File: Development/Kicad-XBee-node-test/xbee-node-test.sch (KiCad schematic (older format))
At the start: 41 parts, among them IC1 ATMEGA48-P

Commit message: Complete Kicad-XBee-node-test PCB to the layout stage. Added some jumpers to allow the board to be used in low power mode. Includes name change.
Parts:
- removed Q?: 2N7002, symbol MOSFET_N
- removed RV?: 10K, symbol POT
- removed U?: 78L05, symbol 78L05
- added Q1: 2N7002, photodiode:SOT23GDS, symbol MOSFET_N
- added R14: 1M, photodiode:SM0603_Resistor, symbol R
- added SW1: Reset, photodiode:SW_PUSH_TINY, symbol SW_Push
- added SW2: Commissioning, photodiode:SW_PUSH_TINY, symbol SW_Push
- added U1: TPS77033, photodiode:SOT23-5, symbol TPS77033
- added W1, W2, W3: Jumper, photodiode:SIL-2, symbol TEST_2P
- C1, C2, C3, C4, C5: renamed from C?; footprint (none) -> photodiode:SM0603_Capa
- C6, C7: renamed from C?; footprint (none) -> photodiode:SM1206POL
- D1: renamed from D?; footprint (none) -> photodiode:TO-92_LM336
- D2, D4, D6, D7: renamed from D?; footprint (none) -> photodiode:LED-5MM
- D3, D5: renamed from D?; footprint (none) -> photodiode:D_0603
- D8: renamed from D?; footprint (none) -> photodiode:D_SOD-323_HandSoldering
- IC1: footprint DIL28 -> photodiode:DIP-28
- L1, L2: renamed from L?; footprint (none) -> photodiode:R_0805
- P1: renamed from P?; footprint (none) -> photodiode:PINHEAD1-6
- P2, P3, P4: renamed from P?; footprint (none) -> photodiode:PINHEAD1-2
- Q2: renamed from Q?; footprint (none) -> photodiode:SOT23GDS
- R1, R10, R11, R12, R13, R2, R7, R8, R9: renamed from R?; footprint (none) -> photodiode:SM0603_Resistor
- R3, R4, R5, R6: renamed from R?; value 270 -> 470; footprint (none) -> photodiode:SM0603_Resistor
- RV1: renamed from RV?; footprint (none) -> photodiode:Potentiometer_Bourns_3362F
- XB1: footprint (none) -> photodiode:XBee
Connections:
- net labels added: On_Sleep
- net labels removed: On/Sleep, Sleep/RQ, VBATT, VBATT_CTL
- wire segments 52 -> 44
- no-connect marks 5 -> 6
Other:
- note added: "31/01/2017"
- note added: "XBee Node test Board"
- moved on the sheet: C1, C7, D2, D4, D6, D7, D8, P2, R3, R4, R5, R6

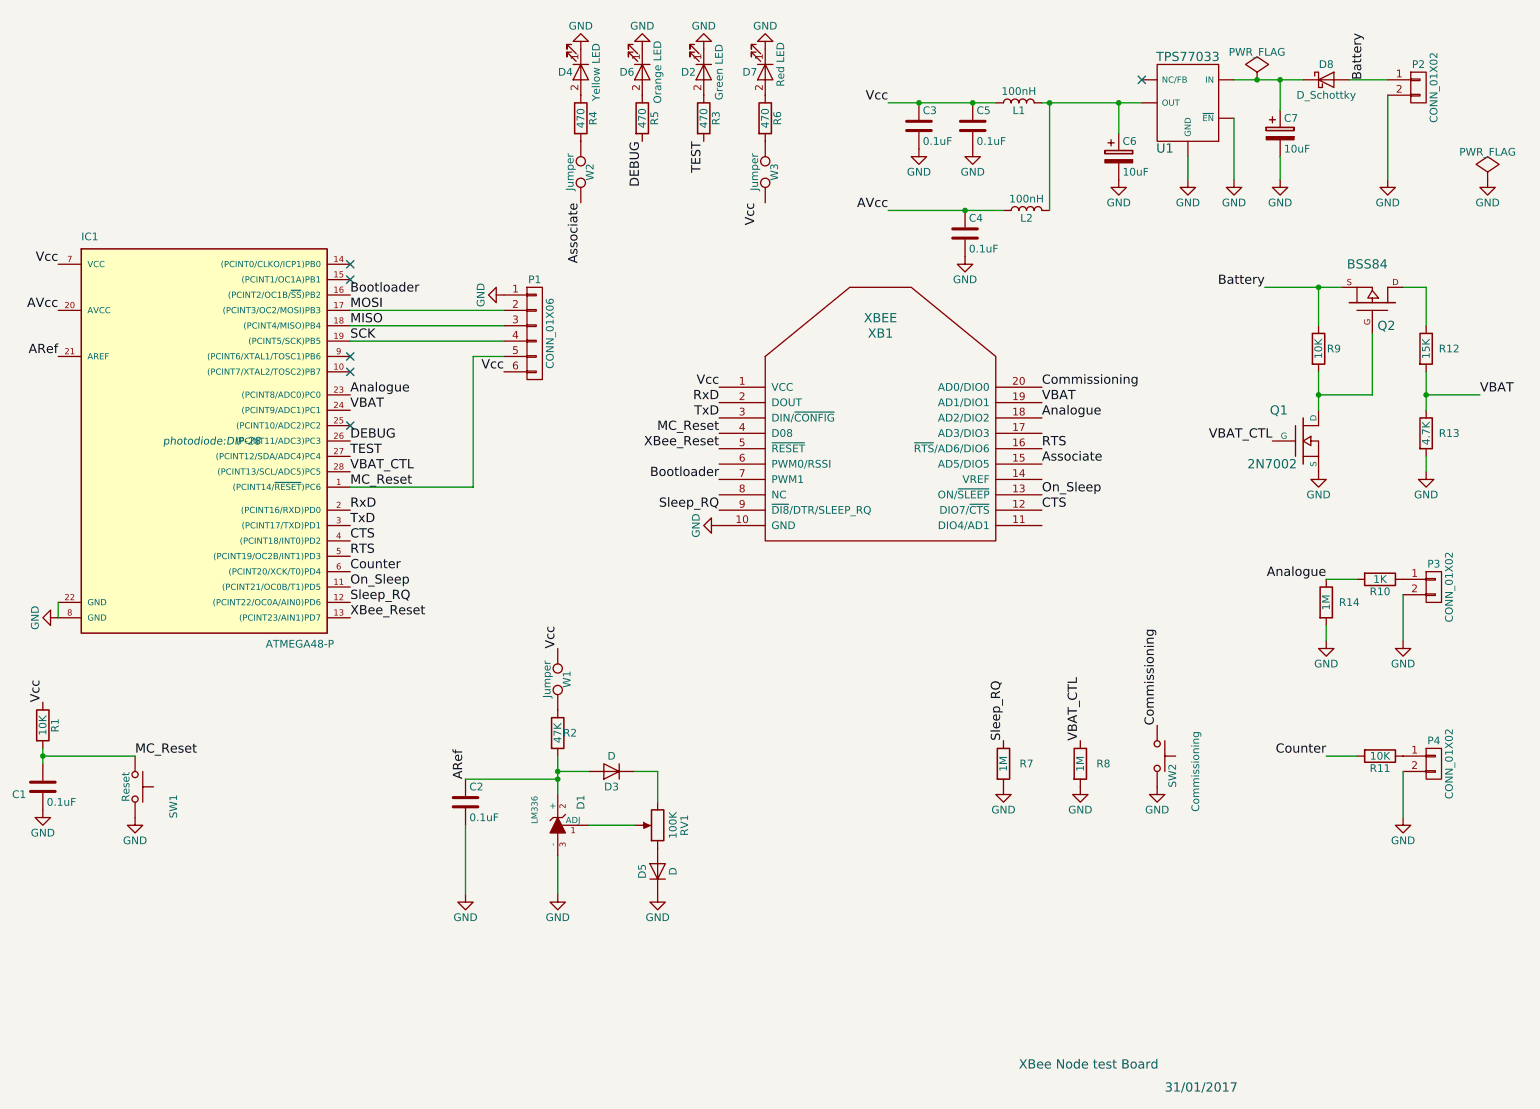
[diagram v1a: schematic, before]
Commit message: Kicad-Xbee-node-test: first draft of PCB
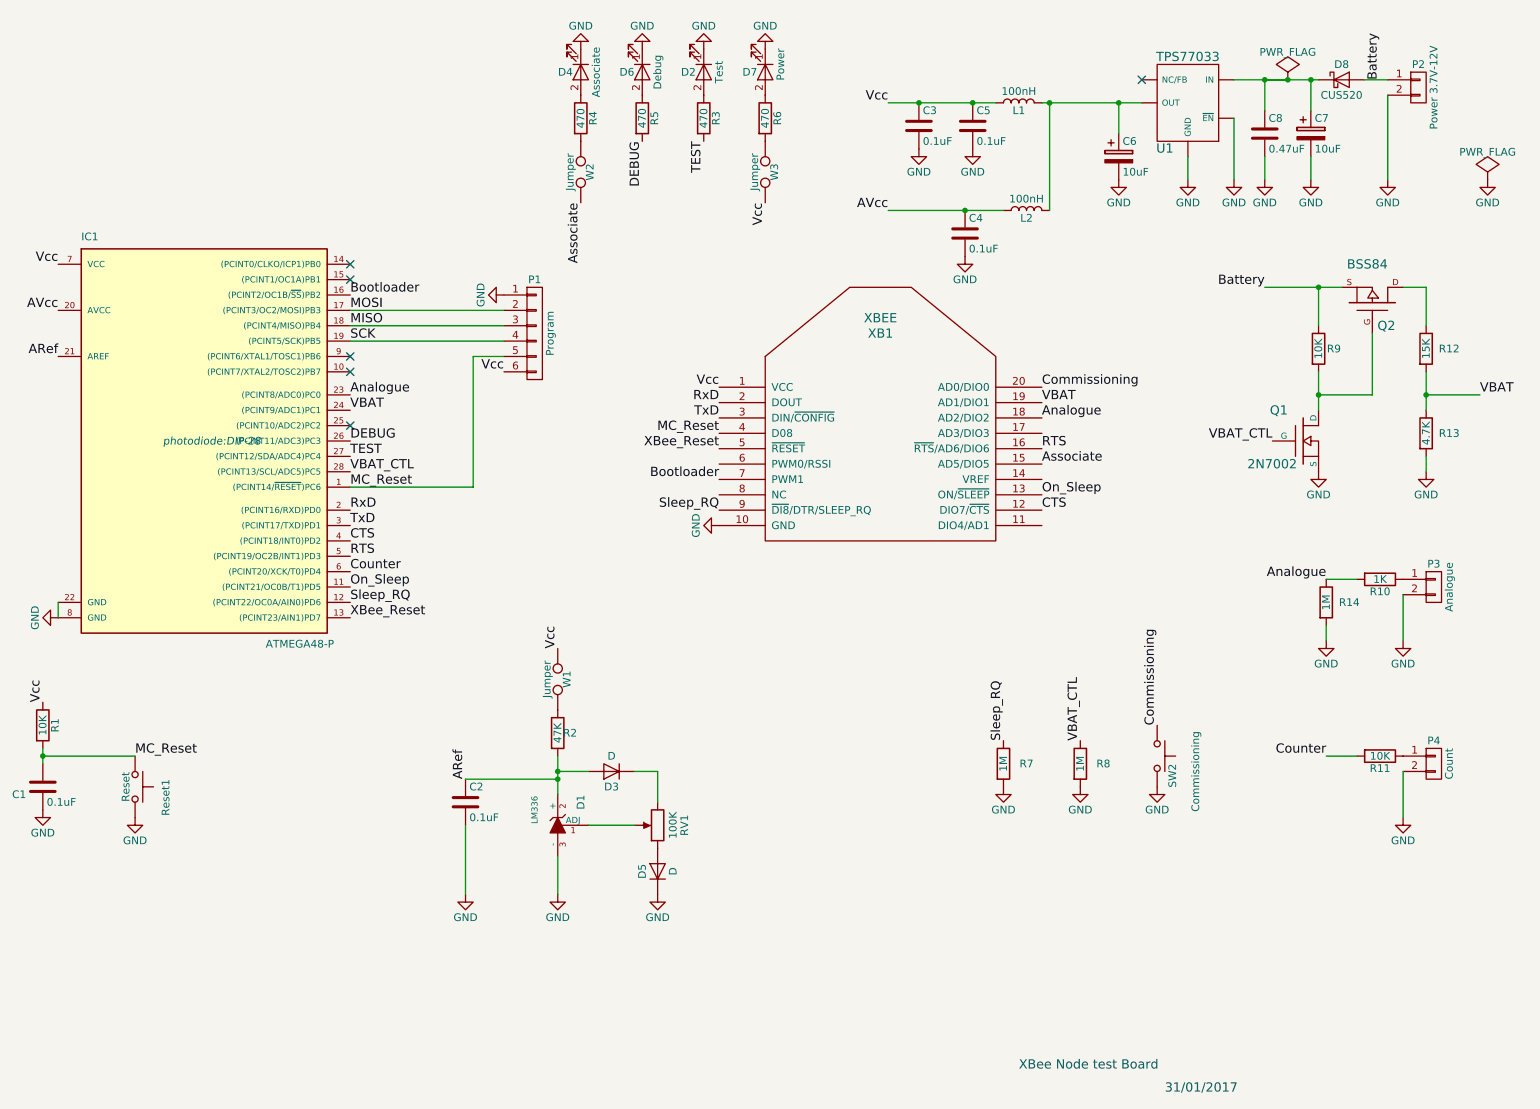
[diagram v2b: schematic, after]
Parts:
- added C8: 0.47uF, photodiode:SM0603_Capa, symbol C
- D2: value Green LED -> Test
- D4: value Yellow LED -> Associate
- D6: value Orange LED -> Debug
- D7: value Red LED -> Power
- D8: value D_Schottky -> CUS520
- P1: value CONN_01X06 -> Program
- P2: value CONN_01X02 -> Power 3.7V-12V
- P3: value CONN_01X02 -> Analogue
- P4: value CONN_01X02 -> Count
- renumbered SW1 to Reset1
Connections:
- net GND: now also C8.2
- net Vcc: now also W3.2
- net at C7.1, D8.1 (K), U1.1 (IN): now also C8.1
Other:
- moved on the sheet: C7, D8
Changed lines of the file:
@@
 P 10150 1100
 F 0 "P2" H 10150 1250 50  0000 C CNN
-F 1 "CONN_01X02" V 10250 1100 50  0000 C CNN
+F 1 "Power 3.7V-12V" V 10250 1100 50  0000 C CNN
 F 2 "photodiode:PINHEAD1-2" H 10150 1100 50  0001 C CNN
 F 3 "" H 10150 1100 50  0000 C CNN
@@
 L D_Schottky D8
 U 1 1 587F2FFE
-P 9550 1050
-F 0 "D8" H 9550 1150 50  0000 C CNN
-F 1 "D_Schottky" H 9550 950 50  0000 C CNN
-F 2 "photodiode:D_SOD-323_HandSoldering" H 9550 1050 50  0001 C CNN
-F 3 "" H 9550 1050 50  0000 C CNN
-	1    9550 1050
+P 9650 1050
+F 0 "D8" H 9650 1150 50  0000 C CNN
+F 1 "CUS520" H 9650 950 50  0000 C CNN
+F 2 "photodiode:D_SOD-323_HandSoldering" H 9650 1050 50  0001 C CNN
+F 3 "" H 9650 1050 50  0000 C CNN
+	1    9650 1050
 	1    0    0    -1
 $EndComp
@@
 L CP C7
 U 1 1 587F3075
-P 9250 1400
-F 0 "C7" H 9275 1500 50  0000 L CNN
-F 1 "10uF" H 9275 1300 50  0000 L CNN
-F 2 "photodiode:SM1206POL" H 9288 1250 50  0001 C CNN
-F 3 "" H 9250 1400 50  0000 C CNN
-	1    9250 1400
+P 9450 1400
+F 0 "C7" H 9475 1500 50  0000 L CNN
+F 1 "10uF" H 9475 1300 50  0000 L CNN
+F 2 "photodiode:SM1206POL" H 9488 1250 50  0001 C CNN
+F 3 "" H 9450 1400 50  0000 C CNN
+	1    9450 1400
 	1    0    0    -1
 $EndComp
@@
 L GND #PWR02
 U 1 1 587F31F3
-P 9250 1700
-F 0 "#PWR02" H 9250 1450 50  0001 C CNN
-F 1 "GND" H 9250 1550 50  0000 C CNN
-F 2 "" H 9250 1700 50  0000 C CNN
-F 3 "" H 9250 1700 50  0000 C CNN
-	1    9250 1700
+P 9150 1700
+F 0 "#PWR02" H 9150 1450 50  0001 C CNN
+F 1 "GND" H 9150 1550 50  0000 C CNN
+F 2 "" H 9150 1700 50  0000 C CNN
+F 3 "" H 9150 1700 50  0000 C CNN
+	1    9150 1700
 	1    0    0    -1
 $EndComp
@@
 P 5900 1000
 F 0 "D7" V 5900 900 50  0000 C CNN
-F 1 "Red LED" H 5850 1100 50  0000 C CNN
+F 1 "Power" H 5850 1100 50  0000 C CNN
 F 2 "photodiode:LED-5MM" H 5900 1000 50  0001 C CNN
 F 3 "" H 5900 1000 50  0000 C CNN
@@
 P 5100 1000
 F 0 "D6" V 5100 900 50  0000 C CNN
-F 1 "Orange LED" H 5100 1100 50  0000 C CNN
+F 1 "Debug" H 5100 1100 50  0000 C CNN
 F 2 "photodiode:LED-5MM" H 5100 1000 50  0001 C CNN
 F 3 "" H 5100 1000 50  0000 C CNN
@@
 P 4700 1000
 F 0 "D4" V 4700 900 50  0000 C CNN
-F 1 "Yellow LED" H 4700 1100 50  0000 C CNN
+F 1 "Associate" H 4700 1100 50  0000 C CNN
 F 2 "photodiode:LED-5MM" H 4700 1000 50  0001 C CNN
 F 3 "" H 4700 1000 50  0000 C CNN
@@
 P 5500 1000
 F 0 "D2" V 5500 900 50  0000 C CNN
-F 1 "Green LED" H 5500 1100 50  0000 C CNN
+F 1 "Test" H 5500 1100 50  0000 C CNN
 F 2 "photodiode:LED-5MM" H 5500 1000 50  0001 C CNN
 F 3 "" H 5500 1000 50  0000 C CNN
@@
 Text Label 5100 1450 3    60   ~ 0
 DEBUG
-Text Label 5850 1850 3    60   ~ 0
+Text Label 5900 1850 3    60   ~ 0
 Vcc
 Text Label 6700 1200 2    60   ~ 0
@@
 VBAT_CTL
 Wire Wire Line
-	9950 1050 9700 1050
-Wire Wire Line
-	8950 1050 9400 1050
-Wire Wire Line
-	9250 1250 9250 1050
-Connection ~ 9250 1050
+	9950 1050 9800 1050
+Wire Wire Line
+	8950 1050 9300 1050
+Wire Wire Line
+	9150 1050 9500 1050
+Connection ~ 9150 1050
 Wire Wire Line
 	7700 1200 8350 1200
@@
 Text Label 9150 2400 2    60   ~ 0
 Battery
-Text Label 9800 1050 1    60   ~ 0
+Text Label 9900 1050 1    60   ~ 0
 Battery
 $Comp
 L PWR_FLAG #FLG011
 U 1 1 587F4D87
-P 9100 1050
-F 0 "#FLG011" H 9100 1145 50  0001 C CNN
-F 1 "PWR_FLAG" H 9100 1230 50  0000 C CNN
-F 2 "" H 9100 1050 50  0000 C CNN
-F 3 "" H 9100 1050 50  0000 C CNN
-	1    9100 1050
+P 9300 1050
+F 0 "#FLG011" H 9300 1145 50  0001 C CNN
+F 1 "PWR_FLAG" H 9300 1230 50  0000 C CNN
+F 2 "" H 9300 1050 50  0000 C CNN
+F 3 "" H 9300 1050 50  0000 C CNN
+	1    9300 1050
 	1    0    0    -1
 $EndComp
@@
 P 10250 4350
 F 0 "P3" H 10250 4500 50  0000 C CNN
-F 1 "CONN_01X02" V 10350 4350 50  0000 C CNN
+F 1 "Analogue" V 10350 4350 50  0000 C CNN
 F 2 "photodiode:PINHEAD1-2" H 10250 4350 50  0001 C CNN
 F 3 "" H 10250 4350 50  0000 C CNN
@@
 P 10250 5500
 F 0 "P4" H 10250 5650 50  0000 C CNN
-F 1 "CONN_01X02" V 10350 5500 50  0000 C CNN
+F 1 "Count" V 10350 5500 50  0000 C CNN
 F 2 "photodiode:PINHEAD1-2" H 10250 5500 50  0001 C CNN
 F 3 "" H 10250 5500 50  0000 C CNN
@@
 P 4400 2700
 F 0 "P1" H 4400 3050 50  0000 C CNN
-F 1 "CONN_01X06" V 4500 2700 50  0000 C CNN
+F 1 "Program" V 4500 2700 50  0000 C CNN
 F 2 "photodiode:PINHEAD1-6" H 4400 2700 50  0001 C CNN
 F 3 "" H 4400 2700 50  0000 C CNN
@@
 VBAT
 $Comp
-L SW_Push SW1
+L SW_Push Reset1
 U 1 1 588EFD34
 P 1800 5650
-F 0 "SW1" H 1850 5900 50  0000 L CNN
+F 0 "Reset1" H 1750 5850 50  0000 L CNN
 F 1 "Reset" H 1800 5590 50  0000 C CNN
 F 2 "photodiode:SW_PUSH_TINY" H 1800 5850 50  0001 C CNN
@@
 	-1   0    0    -1
 $EndComp
-Connection ~ 9100 1050
+Connection ~ 9300 1050
 Connection ~ 8200 1200
 NoConn ~ 8350 1050
@@
 	8950 1300 8950 1700
 Wire Wire Line
-	9250 1700 9250 1550
+	9150 1700 9150 1550
 Wire Wire Line
 	8650 1700 8650 1550
@@
 	0    1    1    0
 $EndComp
+Wire Wire Line
+	9150 1250 9150 1050
+$Comp
+L C C8
+U 1 1 58907DD7
+P 9150 1400
+F 0 "C8" H 9175 1500 50  0000 L CNN
+F 1 "0.47uF" H 9175 1300 50  0000 L CNN
+F 2 "photodiode:SM0603_Capa" H 9188 1250 50  0001 C CNN
+F 3 "" H 9150 1400 50  0000 C CNN
+	1    9150 1400
+	1    0    0    -1
+$EndComp
+$Comp
+L GND #PWR032
+U 1 1 58907FCC
+P 9450 1700
+F 0 "#PWR032" H 9450 1450 50  0001 C CNN
+F 1 "GND" H 9450 1550 50  0000 C CNN
+F 2 "" H 9450 1700 50  0000 C CNN
+F 3 "" H 9450 1700 50  0000 C CNN
+	1    9450 1700
+	1    0    0    -1
+$EndComp
+Wire Wire Line
+	9450 1250 9450 1050
+Connection ~ 9450 1050
+Wire Wire Line
+	9450 1550 9450 1700
 $EndSCHEMATC

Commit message: Minor tweaks on the PCBs ready to manufacture
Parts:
- added P5: VRef, photodiode:SIL-1, symbol CONN_01X01
- added P6: GND, photodiode:SIL-1, symbol CONN_01X01
- L1, L2: symbol L -> INDUCTOR_SMALL
- Reset1, SW2: symbol SW_Push -> SW_PUSH
- W1, W2, W3: symbol TEST_2P -> JUMPER
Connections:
- wire segments 47 -> 46
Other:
- moved on the sheet: C1, C3, C4, C5, RV1

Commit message: Correct some stupid errors in Testboard and XBee-node-test PCBs.
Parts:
- D1: value LM336 -> LM336-2.5V
- D3, D5: value D -> 1N4148
- R2: value 47K -> 2.2K
- R3, R4, R5, R6: value 470 -> 220
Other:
- moved on the sheet: RV1
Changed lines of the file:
@@
 P 5900 1300
 F 0 "R6" V 5980 1300 50  0000 C CNN
-F 1 "470" V 5900 1300 50  0000 C CNN
+F 1 "220" V 5900 1300 50  0000 C CNN
 F 2 "photodiode:SM0603_Resistor" V 5830 1300 50  0001 C CNN
 F 3 "" H 5900 1300 50  0000 C CNN
@@
 P 5100 1300
 F 0 "R5" V 5180 1300 50  0000 C CNN
-F 1 "470" V 5100 1300 50  0000 C CNN
+F 1 "220" V 5100 1300 50  0000 C CNN
 F 2 "photodiode:SM0603_Resistor" V 5030 1300 50  0001 C CNN
 F 3 "" H 5100 1300 50  0000 C CNN
@@
 P 4700 1300
 F 0 "R4" V 4780 1300 50  0000 C CNN
-F 1 "470" V 4700 1300 50  0000 C CNN
+F 1 "220" V 4700 1300 50  0000 C CNN
 F 2 "photodiode:SM0603_Resistor" V 4630 1300 50  0001 C CNN
 F 3 "" H 4700 1300 50  0000 C CNN
@@
 P 5500 1300
 F 0 "R3" V 5580 1300 50  0000 C CNN
-F 1 "470" V 5500 1300 50  0000 C CNN
+F 1 "220" V 5500 1300 50  0000 C CNN
 F 2 "photodiode:SM0603_Resistor" V 5430 1300 50  0001 C CNN
 F 3 "" H 5500 1300 50  0000 C CNN
@@
 U 1 1 588055C4
 P 5200 5900
-F 0 "RV1" V 5150 5750 50  0000 C CNN
-F 1 "100K" V 5250 5750 50  0000 C CNN
+F 0 "RV1" H 5050 5900 50  0000 C CNN
+F 1 "100K" H 5050 5800 50  0000 C CNN
 F 2 "photodiode:Potentiometer_Bourns_3362F" H 5200 5900 50  0001 C CNN
 F 3 "" H 5200 5900 50  0000 C CNN
 	1    5200 5900
-	0    -1   -1   0
+	-1   0    0    1
 $EndComp
 $Comp
@@
 P 4900 5550
 F 0 "D3" H 4900 5650 50  0000 C CNN
-F 1 "D" H 4900 5450 50  0000 C CNN
+F 1 "1N4148" H 4900 5450 50  0000 C CNN
 F 2 "photodiode:D_0603" H 4900 5550 50  0001 C CNN
 F 3 "" H 4900 5550 50  0000 C CNN
@@
 U 1 1 58805780
 P 5200 6200
-F 0 "D5" H 5200 6300 50  0000 C CNN
-F 1 "D" H 5200 6100 50  0000 C CNN
+F 0 "D5" V 5100 6050 50  0000 C CNN
+F 1 "1N4148" V 5200 5950 50  0000 C CNN
 F 2 "photodiode:D_0603" H 5200 6200 50  0001 C CNN
 F 3 "" H 5200 6200 50  0000 C CNN
@@
 U 1 1 58805FCA
 P 4550 5300
-F 0 "R2" H 4630 5300 50  0000 C CNN
-F 1 "47K" V 4550 5300 50  0000 C CNN
+F 0 "R2" H 4650 5300 50  0000 C CNN
+F 1 "2.2K" V 4550 5300 50  0000 C CNN
 F 2 "photodiode:SM0603_Resistor" V 4480 5300 50  0001 C CNN
 F 3 "" H 4550 5300 50  0000 C CNN
@@
 U 1 1 58805B58
 P 4550 5900
-F 0 "D1" H 4700 6050 50  0000 C CNN
-F 1 "LM336" H 4650 5750 40  0000 C CNN
+F 0 "D1" V 4400 6050 50  0000 C CNN
+F 1 "LM336-2.5V" V 4300 6150 40  0000 C CNN
 F 2 "photodiode:TO-92_LM336" H 4550 5900 60  0001 C CNN
 F 3 "" H 4550 5900 60  0000 C CNN
@@
 L CONN_01X01 P5
 U 1 1 58931DA2
-P 5200 5350
-F 0 "P5" V 5200 5450 50  0000 C CNN
-F 1 "VRef" V 5300 5350 50  0000 C CNN
-F 2 "photodiode:SIL-1" H 5200 5350 50  0001 C CNN
-F 3 "" H 5200 5350 50  0000 C CNN
-	1    5200 5350
+P 4250 5400
+F 0 "P5" V 4250 5500 50  0000 C CNN
+F 1 "VRef" V 4350 5400 50  0000 C CNN
+F 2 "photodiode:SIL-1" H 4250 5400 50  0001 C CNN
+F 3 "" H 4250 5400 50  0000 C CNN
+	1    4250 5400
 	0    -1   -1   0
 $EndComp
@@
 	1    0    0    -1
 $EndComp
+Connection ~ 4250 5600
 $EndSCHEMATC

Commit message: Update XBee symbol in node-test and mounts PCB schematics.
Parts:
- removed XB1: XBEE, photodiode:XBee, symbol XBEE
- added XB1: XBEE-ZB, photodiode:XBee, symbol XBEE-ZB
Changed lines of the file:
@@
 $EndDescr
-$Comp
-L XBEE XB1
-U 1 1 587EF6B8
-P 6650 3500
-F 0 "XB1" H 6650 4300 60  0000 C CNN
-F 1 "XBEE" H 6650 4400 60  0000 C CNN
-F 2 "photodiode:XBee" H 6650 3500 60  0001 C CNN
-F 3 "" H 6650 3500 60  0000 C CNN
-	1    6650 3500
-	1    0    0    -1
-$EndComp
 $Comp
 L ATMEGA48-P IC1
@@
 F 0 "IC1" H 1450 4700 50  0000 L BNN
 F 1 "ATMEGA48-P" H 2650 2050 50  0000 L BNN
-F 2 "photodiode:DIP-28" H 2300 3400 50  0000 C CIN
+F 2 "photodiode:DIP-28" H 1850 3450 50  0000 C CIN
 F 3 "" H 2300 3400 50  0000 C CNN
 	1    2300 3400
@@
 $EndComp
 Connection ~ 4250 5600
+$Comp
+L XBEE-ZB XB1
+U 1 1 58B76E4B
+P 6650 3500
+F 0 "XB1" H 6650 4300 60  0000 C CNN
+F 1 "XBEE-ZB" H 6650 4400 60  0000 C CNN
+F 2 "photodiode:XBee" H 6450 2450 60  0001 C CNN
+F 3 "" H 6650 3500 60  0000 C CNN
+	1    6650 3500
+	1    0    0    -1
+$EndComp
 $EndSCHEMATC
